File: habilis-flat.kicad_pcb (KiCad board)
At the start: 2 copper layers, 167.6 x 168.5 mm, 73 parts, among them J1 AudioJack4, SW1 MX, SW10 MX, SW11 MX, SW12 MX, SW13 MX, SW14 MX, SW15 MX, SW16 MX, SW17 MX, SW18 MX, SW19 MX, SW2 MX, SW20 MX, SW21 MX, SW22 MX, SW23 MX, SW24 MX, SW25 MX, SW26 MX, SW27 MX, SW28 MX, SW29 MX, SW3 MX, SW30 MX, SW31 MX, SW32 MX, SW33 MX, SW34 MX, SW35 MX, SW4 MX, SW5 MX, SW6 MX, SW7 MX, SW8 MX, SW9 MX, U1 ProMicro

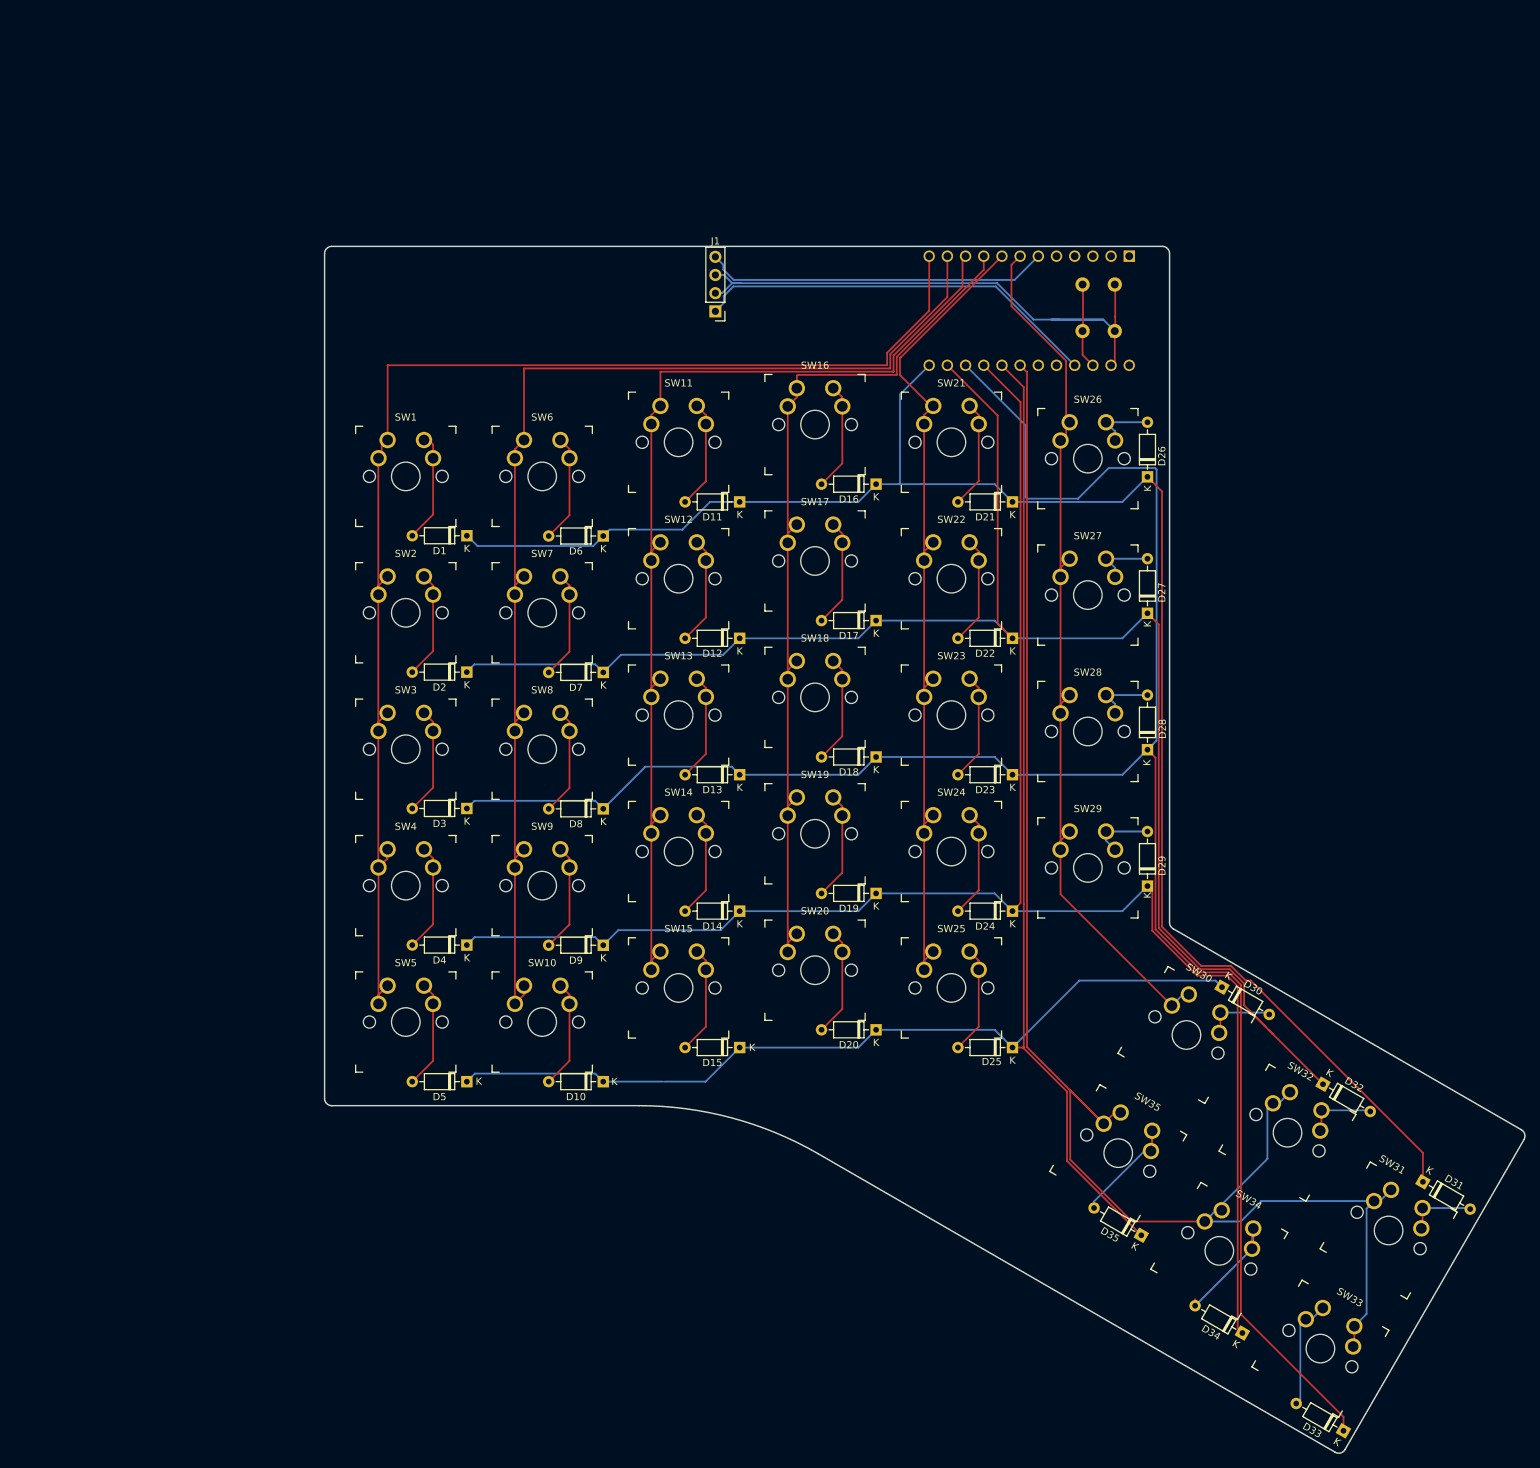
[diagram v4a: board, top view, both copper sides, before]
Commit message: Redraw board shape, fix spacing mistakes
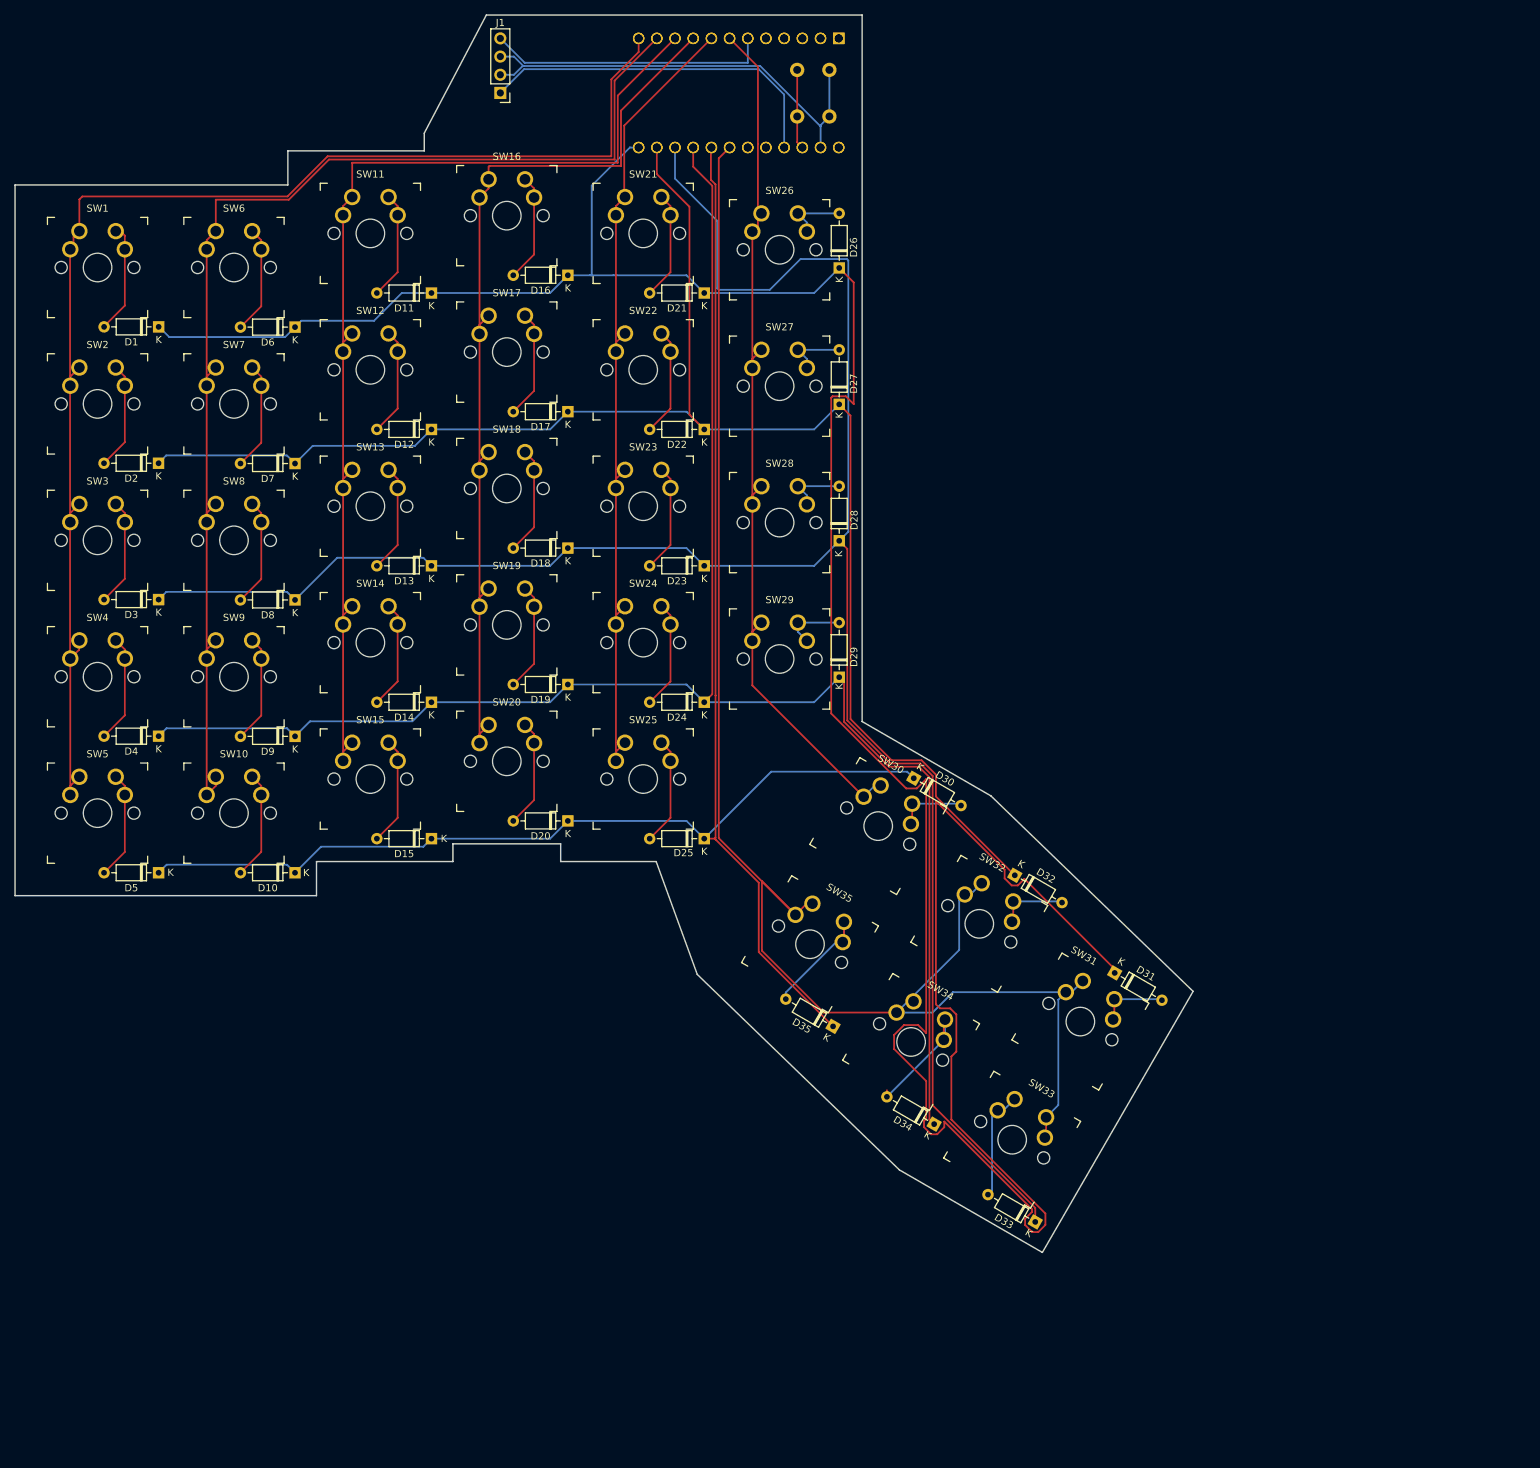
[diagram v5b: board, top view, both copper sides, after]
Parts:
- added U1: ProMicro, promicro:ProMicro-NoSilk, F.Cu at (87.0, -19.3)
- moved D26 52.0 mm to (101.0, 5.14)
- moved D28 52.0 mm to (101.0, 43.2)
- moved SW27 52.0 mm to (95.2, 16.6)
- moved D11 52.0 mm to (44.1, 8.64)
- moved D12 52.0 mm to (44.1, 27.7)
- moved D13 52.0 mm to (44.1, 46.7)
- moved D17 52.0 mm to (63.1, 25.2)
- moved D18 52.0 mm to (63.1, 44.3)
- moved D20 52.0 mm to (63.1, 82.4)
- moved D3 52.0 mm to (5.99, 51.5)
- moved D4 52.0 mm to (5.99, 70.5)
- moved SW1 52.0 mm to (0.00, 0.00)
- moved SW11 52.0 mm to (38.1, -4.76)
- moved SW12 52.0 mm to (38.1, 14.3)
- moved SW13 52.0 mm to (38.1, 33.3)
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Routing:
- net Net-(D1-K): track 237.6 -> 396.7 mm
- net Net-(J1-PadR1): track 83.9 -> 63.9 mm
- net Net-(U1-SCL): track 48.2 -> 39.4 mm
- net Net-(U1-VCC): track 56.8 -> 49.9 mm
- net Net-(U1-E6): track 149.3 -> 154.2 mm
- net Net-(U1-D7): track 128.9 -> 133.8 mm
- net Net-(D12-K): track 225.6 -> 221.9 mm
- net Net-(U1-C6): track 120.5 -> 118.8 mm
- net Net-(U1-B4): track 171.8 -> 173.4 mm
- net Net-(U1-F6): track 225.3 -> 226.7 mm
- net Net-(U1-B5): track 189.9 -> 191.3 mm
- net Net-(U1-D4): track 127.7 -> 126.9 mm
- net Net-(U1-RST): track 11.9 -> 11.1 mm
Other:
- board size 167.6 x 168.5 mm -> 164.5 x 172.8 mm
- board text added: "FLAT"
